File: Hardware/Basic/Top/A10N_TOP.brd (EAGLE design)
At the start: 38 x 38 mm, 64 parts, among them SW1 SWITCH.MOM, SW2 SWITCH.MOM, U2 NRF52832_MODULE_MDBT42, U4 PCF8523, U5 FT231XS

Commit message: Added bottom board
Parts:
- moved J2 26.7 mm to (2.13, 19.7), turned to 270 degrees
- moved SW1 10.2 mm to (32.0, 3.96)
- moved SW2 10.1 mm to (22.0, 3.94)
- moved C6 9.48 mm to (16.2, -4.27)
- moved R15 9.03 mm to (19.0, -4.24)
- moved R12 6.18 mm to (13.5, 6.15)
- moved C5 4.44 mm to (11.6, 2.49)
- moved LDO2 4.26 mm to (14.9, 2.36)
- moved C21 4.18 mm to (26.1, 12.5)
- moved C12 3.77 mm to (20.5, 18.8)
- moved D4 3.51 mm to (7.70, 3.91)
- moved D5 3.50 mm to (7.72, 1.50)
- moved L2 2.33 mm to (20.2, 24.7)
- moved C20 2.17 mm to (14.6, 10.3)
- moved R11 2.14 mm to (19.6, 13.1)
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
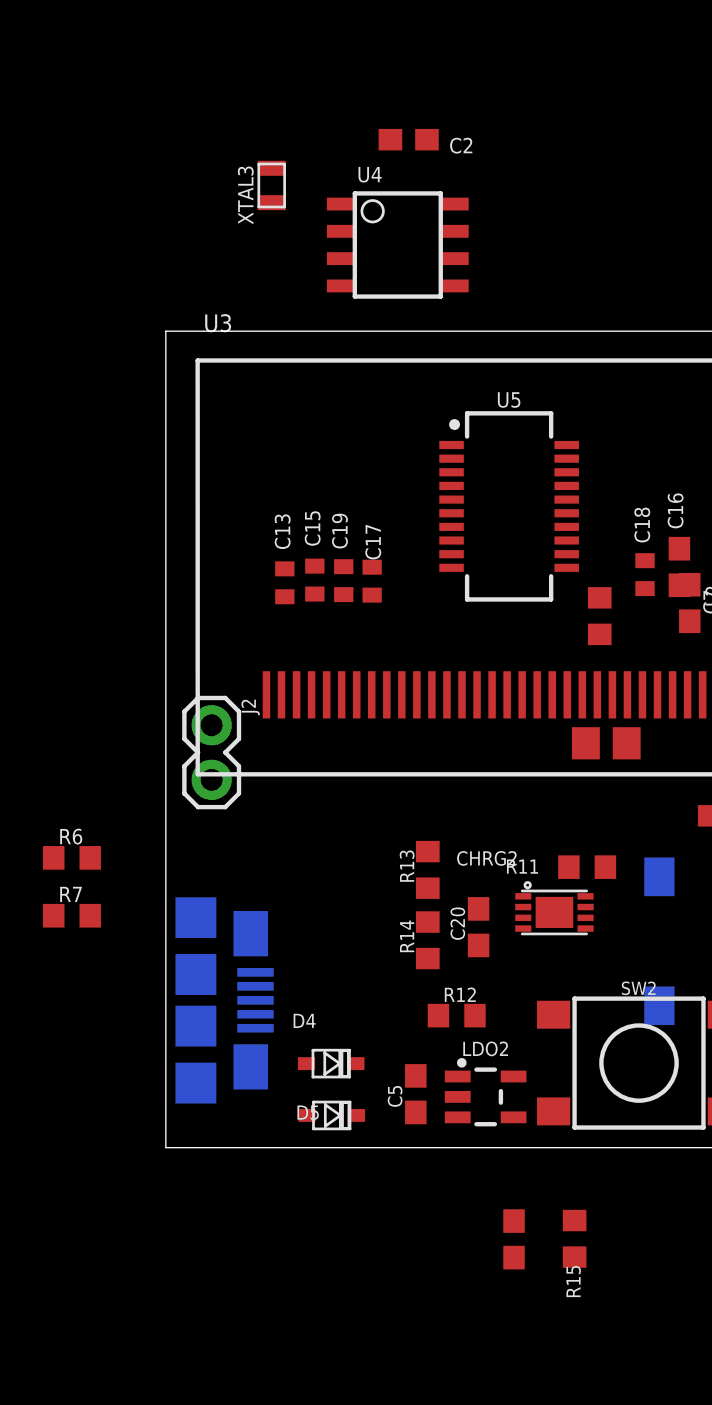
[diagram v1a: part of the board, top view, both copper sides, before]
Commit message: Connected SD Card, LEDs,
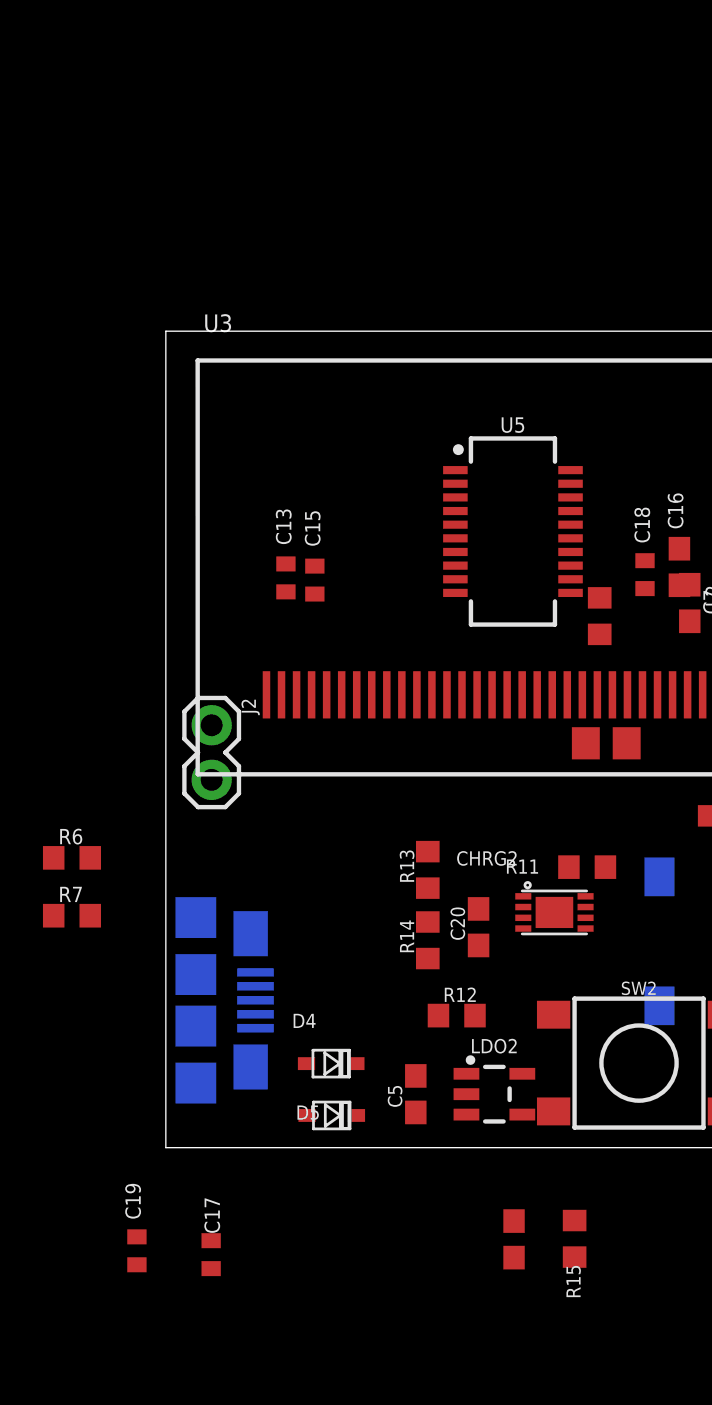
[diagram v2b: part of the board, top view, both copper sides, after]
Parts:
- removed C2: 1u, LinnesLab-Passives:C0603
- removed U4: PCF8523, LinnesLab-Clocks:SO8
- removed XTAL3: 32.7680kHz, LinnesLab-Clocks:2-SMD.NOLEAD.2.0MMTO1.2MM
- moved C19 32.6 mm to (-1.35, -4.80)
- moved C17 32.2 mm to (2.11, -4.98)
- moved U5 1.18 mm to (16.2, 28.7)
- moved LDO2 0.43 mm to (15.3, 2.49)
- moved C13 0.23 mm to (5.59, 26.5)
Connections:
- removed net BATT: R13.1, R14.2
- removed net CD1: SD2.CD1
- removed net CHRG.STAT: CHRG2.5, R12.1
- removed net CS.OLED: U3.13
- removed net DC.OLED: U3.15
- removed net N$19: U4.2, XTAL3.P$1
- removed net N$20: U4.1, XTAL3.P$2
- removed net RESET.OLED: U3.14
- removed net SD.CS: SD2.2
- removed net VBATT: U4.3
- new net A4/BATT_STATUS: R13.1, R14.2, U2.5
- new net A6/TIA: U2.7
- new net A7/PPG: U2.8
- new net D11/SW2: SW2.A1, U2.25
- new net D15/SW1: SW1.A1, U2.29
- new net D16/CS_OLED: U2.30, U3.13
- new net D27/CHRG_STATUS: CHRG2.5, R12.1, U2.4
- new net D29/LED_CTRL: U2.6
- new net D3/RESET_OLED: U2.16, U3.14
- new net D4/DC_OLED: U2.17, U3.15
- new net D5/CRD_DETECT: SD2.CD1, U2.18
- new net D7/SD_CS: SD2.2, U2.20
- new net N$27: U2.15
- net 3.3V: no longer C2.1, U4.8
- net GND: now also SW1.B1, SW1.B2, SW2.B1, SW2.B2; no longer C2.2, U4.4
- net SCL: no longer U4.6
- net SDA: no longer U4.5

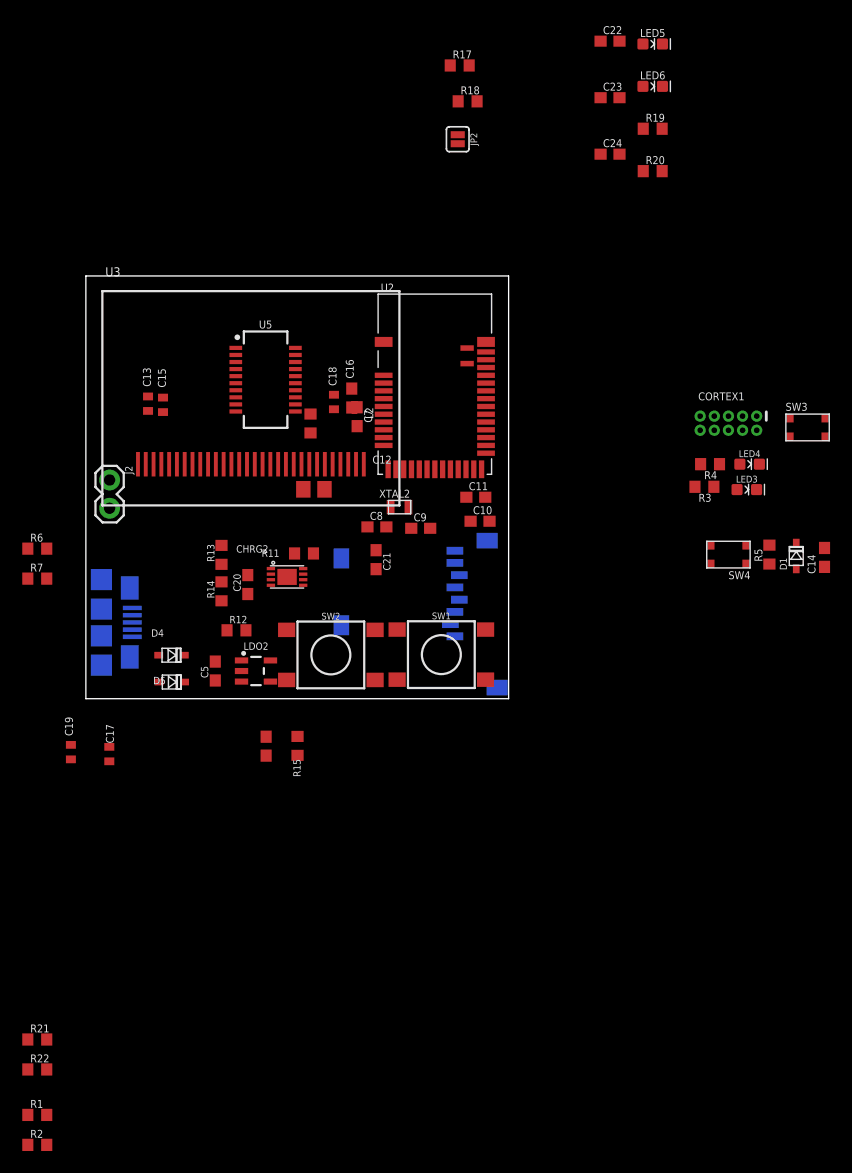
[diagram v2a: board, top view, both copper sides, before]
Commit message: Added PPG and Bottom Boards
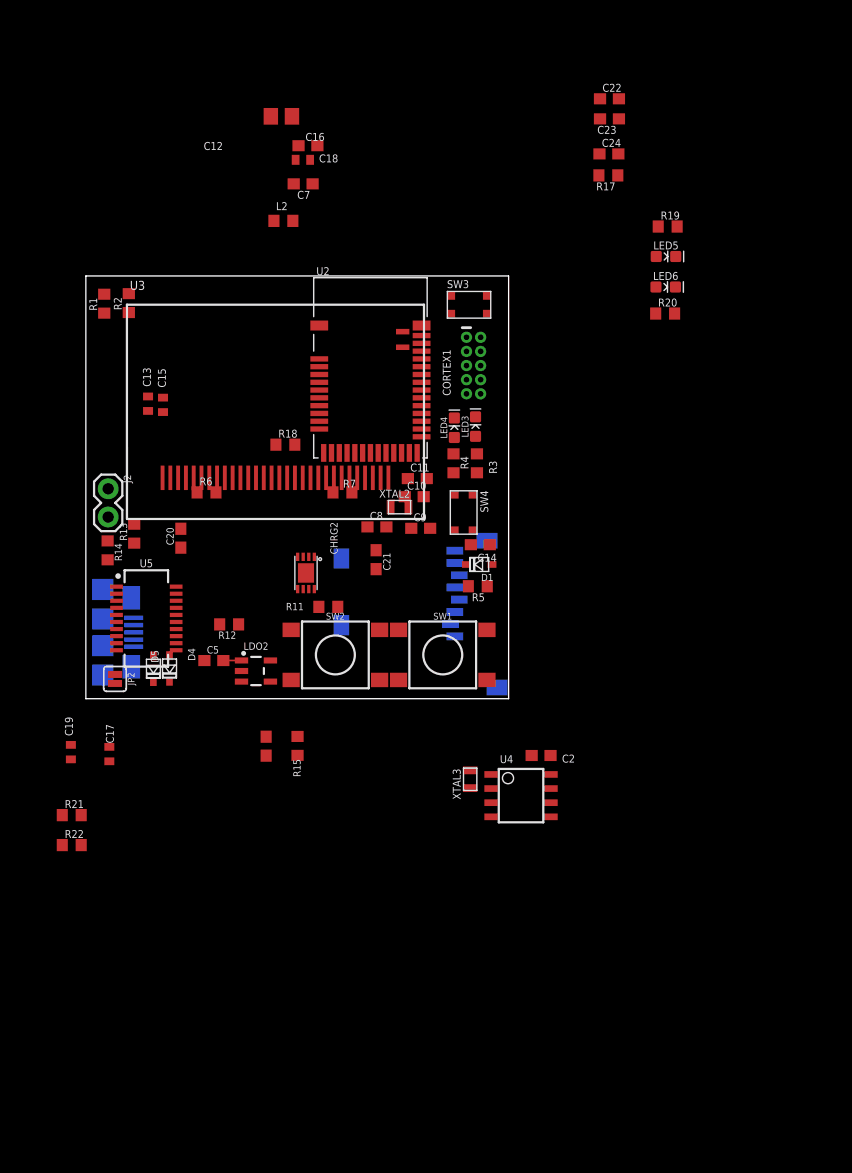
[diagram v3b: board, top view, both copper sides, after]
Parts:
- added C2: 1u, LinnesLab-Passives:C0603
- added U4: PCF8523, LinnesLab-Clocks:SO8
- added XTAL3: 32.7680kHz, LinnesLab-Clocks:2-SMD.NOLEAD.2.0MMTO1.2MM
- moved R2 76.1 mm to (3.86, 35.6), turned to 90 degrees
- moved R1 73.2 mm to (1.65, 35.5), turned to 90 degrees
- moved JP2 57.5 mm to (2.62, 1.78)
- moved R18 34.9 mm to (17.9, 22.8)
- moved C12 33.7 mm to (17.6, 52.3), turned to 180 degrees
- moved SW3 32.4 mm to (34.4, 35.4)
- moved C14 31.0 mm to (35.5, 13.8), turned to 0 degrees
- moved D1 28.5 mm to (35.4, 12.1), turned to 180 degrees
- moved R7 28.5 mm to (23.1, 18.5)
- moved LED4 26.7 mm to (33.1, 24.4), turned to 90 degrees
- moved R5 26.4 mm to (35.2, 10.1), turned to 180 degrees
- moved LED3 25.0 mm to (35.0, 24.5), turned to 90 degrees
- moved SW4 24.1 mm to (34.0, 16.7), turned to 270 degrees
- moved U5 24.0 mm to (5.44, 7.21)
- moved CORTEX1 23.5 mm to (34.8, 29.9), turned to 270 degrees
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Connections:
- removed net SCL: R2.1, U2.3
- removed net SDA: R1.1, U2.2
- new net D25/SDA: R1.1, U2.2, U4.5
- new net D26/SCL: R2.1, U2.3, U4.6
- new net N$28: U4.2, XTAL3.P$1
- new net N$29: U4.1, XTAL3.P$2
- new net VBAT: U4.3
- net 3.3V: now also C2.1, U4.8
- net GND: now also C2.2, U4.4
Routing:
- net VIN: track 0.00 -> 1.64 mm
